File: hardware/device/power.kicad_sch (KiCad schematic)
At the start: 32 parts, among them J2 USB, U1 VOL_PWR_POT, U20 TPS62A02DRL, U21 TPS560200, U22 MAX17261xxTD, U23 BQ21040DBV, U26 FUSB303BTMX, U27 FUSB302B01MPX

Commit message: feat: add various connectors
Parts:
- added J1: POT_CONN, pocket_synth:CONN_503480-0540_MOL, symbol pocket_synth:5034800540
- added J4: FX6-20P-0.8SV1(71), pocket_synth:FX6-20P-0.8SV1(71), symbol pocket_synth:FX6-20P-0.8SV1(71)
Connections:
- net GND: now also J1.6 (MP), J1.7 (MP)
- net MCU_PWR_SW: now also J1.2; no longer U1.5 (SW)
- net VDD: now also J1.1; no longer U1.4 (SW)
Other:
- moved on the sheet: U1

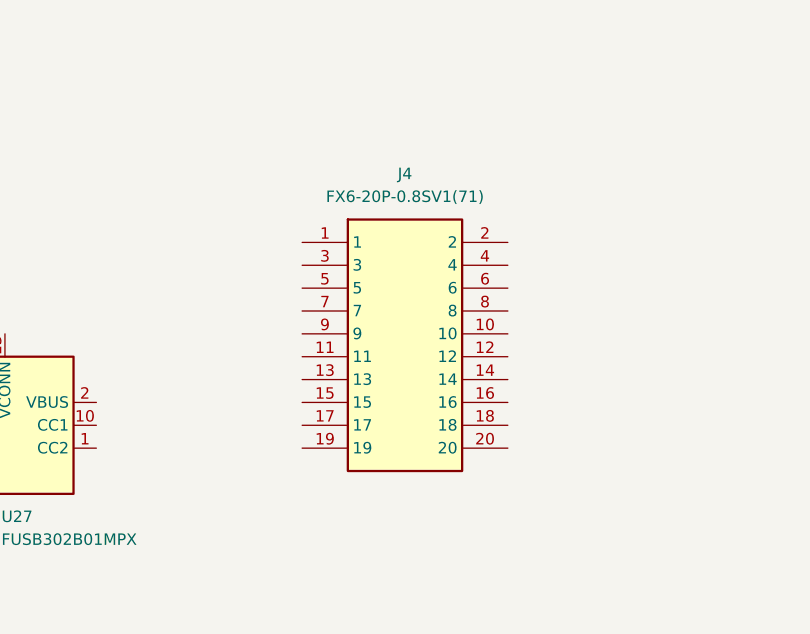
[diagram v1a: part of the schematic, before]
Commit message: feat: audio schematic, FMC bus, SDRAM connections
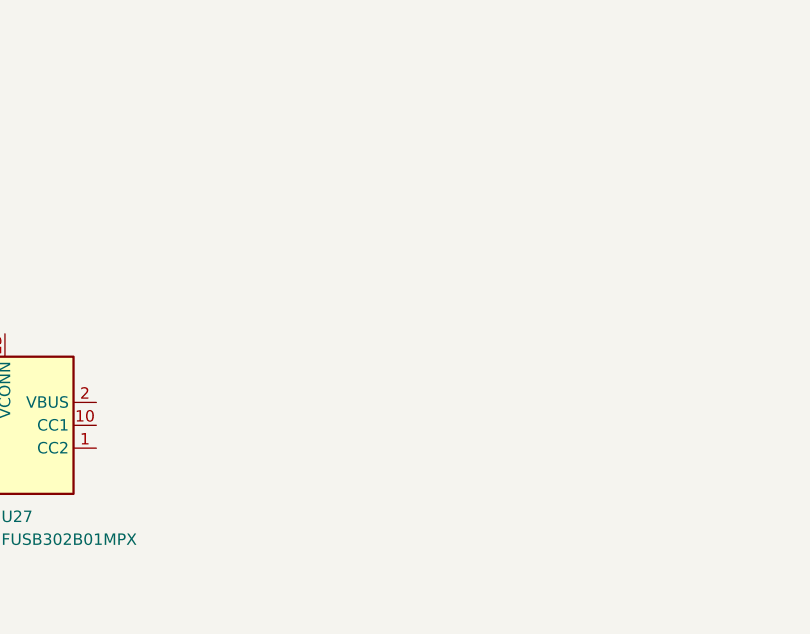
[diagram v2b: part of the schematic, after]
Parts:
- removed J4: FX6-20P-0.8SV1(71), pocket_synth:FX6-20P-0.8SV1(71), symbol pocket_synth:FX6-20P-0.8SV1(71)
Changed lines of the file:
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@@
-	)
-	(symbol
-		(lib_id "pocket_synth:FX6-20P-0.8SV1(71)")
-		(at 85.09 100.33 0)
-		(unit 1)
-		(exclude_from_sim no)
-		(in_bom yes)
-		(on_board yes)
-		(dnp no)
-		(fields_autoplaced yes)
-		(property "Reference" "J4"
-			(at 85.09 81.28 0)
-			(effects
-				(font
-					(size 1.27 1.27)
-				)
-			)
-		)
-		(property "Value" "FX6-20P-0.8SV1(71)"
-			(at 85.09 83.82 0)
-			(effects
-				(font
-					(size 1.27 1.27)
-				)
-			)
-		)
-		(property "Footprint" "pocket_synth:FX6-20P-0.8SV1(71)"
-			(at 92.71 183.82 0)
-			(effects
-				(font
-					(size 1.27 1.27)
-				)
-				(justify left top)
-				(hide yes)
-			)
-		)
-		(property "Datasheet" "https://www.hirose.com/en/product/p/CL0576-0021-0-71"
-			(at 92.71 283.82 0)
-			(effects
-				(font
-					(size 1.27 1.27)
-				)
-				(justify left top)
-				(hide yes)
-			)
-		)
-		(property "Description" "Hirose FX6 Series, 0.8mm Pitch 20 Way 2 Row Straight PCB Header, Solder Termination, 0.5A"
-			(at 85.09 100.33 0)
-			(effects
-				(font
-					(size 1.27 1.27)
-				)
-				(hide yes)
-			)
-		)
-		(property "Height" "6.25"
-			(at 92.71 483.82 0)
-			(effects
-				(font
-					(size 1.27 1.27)
-				)
-				(justify left top)
-				(hide yes)
-			)
-		)
-		(property "Mouser Part Number" "798-FX620P08SV171"
-			(at 92.71 583.82 0)
-			(effects
-				(font
-					(size 1.27 1.27)
-				)
-				(justify left top)
-				(hide yes)
-			)
-		)
-		(property "Mouser Price/Stock" "https://www.mouser.co.uk/ProductDetail/Hirose-Connector/FX6-20P-0.8SV171?qs=zOgoZG1CgI%2FdLW6QquT0oA%3D%3D"
-			(at 92.71 683.82 0)
-			(effects
-				(font
-					(size 1.27 1.27)
-				)
-				(justify left top)
-				(hide yes)
-			)
-		)
-		(property "Manufacturer_Name" "Hirose"
-			(at 92.71 783.82 0)
-			(effects
-				(font
-					(size 1.27 1.27)
-				)
-				(justify left top)
-				(hide yes)
-			)
-		)
-		(property "Manufacturer_Part_Number" "FX6-20P-0.8SV1(71)"
-			(at 92.71 883.82 0)
-			(effects
-				(font
-					(size 1.27 1.27)
-				)
-				(justify left top)
-				(hide yes)
-			)
-		)
-		(pin "16"
-		)
-		(pin "5"
-		)
-		(pin "12"
-		)
-		(pin "3"
-		)
-		(pin "15"
-		)
-		(pin "19"
-		)
-		(pin "10"
-		)
-		(pin "18"
-		)
-		(pin "14"
-		)
-		(pin "8"
-		)
-		(pin "1"
-		)
-		(pin "6"
-		)
-		(pin "4"
-		)
-		(pin "13"
-		)
-		(pin "2"
-		)
-		(pin "17"
-		)
-		(pin "11"
-		)
-		(pin "7"
-		)
-		(pin "9"
-		)
-		(pin "20"
-		)
-		(instances
-			(project ""
-				(path "/485383b8-00f4-4405-b270-de249939cff4/4ddef61a-efa7-4012-86d6-37c4f1088d14"
-					(reference "J4")
-					(unit 1)
-				)
-			)
-		)
 	)
 	(symbol

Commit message: feat: various layouts, changed SDRAM to BGA
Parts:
- removed C42: 10uf, Capacitor_SMD:C_0603_1608Metric_Pad1.08x0.95mm_HandSolder, symbol Device:C_Small
- removed U1: VOL_PWR_POT, pocket_synth:PTR901-2015K-B103, symbol pocket_synth:PTR901-2015K-B103
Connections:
- net GND: now also R2.2
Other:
- note added: "1v8 500mA Digital Supply"
- note added: "3v3 2A Digital Supply"
- note added: "Soft-Power Circuit & Volume Pot"
- note removed: "1v8 500mA Supply"
- note removed: "3v3 2A Supply"
- note removed: "TODO: MIDI over USB-C additional lines?"
- note removed: "TODO: ribbon cable connector"
- moved on the sheet: BT1, D17, D18, D19, J1, R1, R2, R3

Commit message: feat: various audio and power schematic layout
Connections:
- net USB_D+: now reaches J2.A6 (D+)
- net USB_D+: now also J2.B6 (D+)
- net USB_D-: now reaches J2.A7 (D-)
- net USB_D-: now also J2.B7 (D-)
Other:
- note added: "3.6-5.2v unregulated battery/charge voltage"
- note removed: "3.6-5.2v battery/charge voltage"
- moved on the sheet: D18, D19, J1, R1, R3

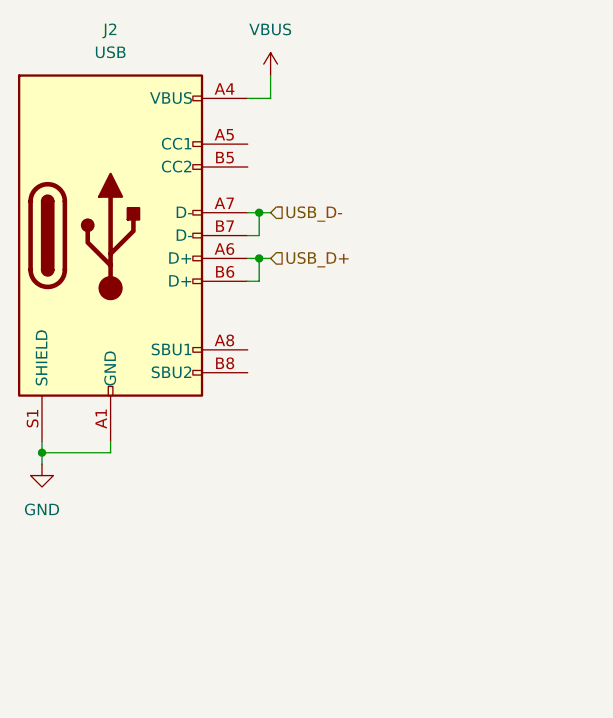
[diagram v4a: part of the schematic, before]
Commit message: feat: add audio routing muxes
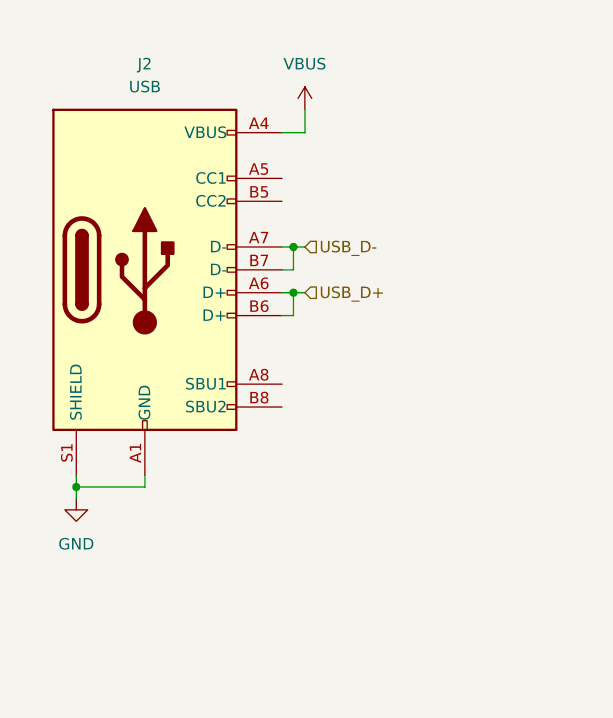
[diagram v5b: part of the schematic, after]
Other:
- moved on the sheet: J2
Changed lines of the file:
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@@
 	)
 	(junction
-		(at 17.78 62.23)
+		(at 21.59 66.04)
 		(diameter 0)
 		(color 0 0 0 0)
@@
 	)
 	(junction
-		(at 41.91 35.56)
+		(at 45.72 39.37)
 		(diameter 0)
 		(color 0 0 0 0)
 	)
 	(junction
-		(at 41.91 40.64)
+		(at 45.72 44.45)
 		(diameter 0)
 		(color 0 0 0 0)
@@
 	(wire
 		(pts
-			(xy 41.91 43.18) (xy 40.64 43.18)
+			(xy 45.72 46.99) (xy 44.45 46.99)
 		)
 		(stroke
@@
 	(wire
 		(pts
-			(xy 43.18 20.32) (xy 43.18 22.86)
+			(xy 46.99 24.13) (xy 46.99 26.67)
 		)
 		(stroke
@@
 	(wire
 		(pts
-			(xy 17.78 62.23) (xy 25.4 62.23)
+			(xy 21.59 66.04) (xy 29.21 66.04)
 		)
 		(stroke
@@
 	(wire
 		(pts
-			(xy 40.64 22.86) (xy 43.18 22.86)
+			(xy 44.45 26.67) (xy 46.99 26.67)
 		)
 		(stroke
@@
 	(wire
 		(pts
-			(xy 25.4 60.96) (xy 25.4 62.23)
+			(xy 29.21 64.77) (xy 29.21 66.04)
 		)
 		(stroke
@@
 	(wire
 		(pts
-			(xy 41.91 35.56) (xy 43.18 35.56)
+			(xy 45.72 39.37) (xy 46.99 39.37)
 		)
 		(stroke
@@
 	(wire
 		(pts
-			(xy 41.91 40.64) (xy 41.91 43.18)
+			(xy 45.72 44.45) (xy 45.72 46.99)
 		)
 		(stroke
@@
 	(wire
 		(pts
-			(xy 17.78 60.96) (xy 17.78 62.23)
+			(xy 21.59 64.77) (xy 21.59 66.04)
 		)
 		(stroke
@@
 	(wire
 		(pts
-			(xy 17.78 62.23) (xy 17.78 63.5)
+			(xy 21.59 66.04) (xy 21.59 67.31)
 		)
 		(stroke
@@
 	(wire
 		(pts
-			(xy 40.64 38.1) (xy 41.91 38.1)
+			(xy 44.45 41.91) (xy 45.72 41.91)
 		)
 		(stroke
@@
 	(wire
 		(pts
-			(xy 40.64 35.56) (xy 41.91 35.56)
+			(xy 44.45 39.37) (xy 45.72 39.37)
 		)
 		(stroke
@@
 	(wire
 		(pts
-			(xy 41.91 35.56) (xy 41.91 38.1)
+			(xy 45.72 39.37) (xy 45.72 41.91)
 		)
 		(stroke
@@
 	(wire
 		(pts
-			(xy 41.91 40.64) (xy 43.18 40.64)
+			(xy 45.72 44.45) (xy 46.99 44.45)
 		)
 		(stroke
@@
 	(wire
 		(pts
-			(xy 40.64 40.64) (xy 41.91 40.64)
+			(xy 44.45 44.45) (xy 45.72 44.45)
 		)
 		(stroke
@@
 	(hierarchical_label "USB_D+"
 		(shape input)
-		(at 43.18 40.64 0)
+		(at 46.99 44.45 0)
 		(effects
 			(font
@@
 	(hierarchical_label "USB_D-"
 		(shape input)
-		(at 43.18 35.56 0)
+		(at 46.99 39.37 0)
 		(effects
 			(font
@@
 	(symbol
 		(lib_id "power:GND")
-		(at 17.78 63.5 0)
+		(at 21.59 67.31 0)
 		(unit 1)
 		(exclude_from_sim no)
@@
 		(fields_autoplaced yes)
 		(property "Reference" "#PWR04"
-			(at 17.78 69.85 0)
+			(at 21.59 73.66 0)
 			(effects
 				(font
@@
 		)
 		(property "Value" "GND"
-			(at 17.78 68.58 0)
+			(at 21.59 72.39 0)
 			(effects
 				(font
@@
 		)
 		(property "Footprint" ""
-			(at 17.78 63.5 0)
+			(at 21.59 67.31 0)
 			(effects
 				(font
@@
 		)
 		(property "Datasheet" ""
-			(at 17.78 63.5 0)
+			(at 21.59 67.31 0)
 			(effects
 				(font
@@
 		)
 		(property "Description" "Power symbol creates a global label with name \"GND\" , ground"
-			(at 17.78 63.5 0)
+			(at 21.59 67.31 0)
 			(effects
 				(font
@@
 	(symbol
 		(lib_id "power:VBUS")
-		(at 43.18 20.32 0)
+		(at 46.99 24.13 0)
 		(unit 1)
 		(exclude_from_sim no)
@@
 		(fields_autoplaced yes)
 		(property "Reference" "#PWR05"
-			(at 43.18 24.13 0)
+			(at 46.99 27.94 0)
 			(effects
 				(font
@@
 		)
 		(property "Value" "VBUS"
-			(at 43.18 15.24 0)
+			(at 46.99 19.05 0)
 			(effects
 				(font
@@
 		)
 		(property "Footprint" ""
-			(at 43.18 20.32 0)
+			(at 46.99 24.13 0)
 			(effects
 				(font
@@
 		)
 		(property "Datasheet" ""
-			(at 43.18 20.32 0)
+			(at 46.99 24.13 0)
 			(effects
 				(font
@@
 		)
 		(property "Description" "Power symbol creates a global label with name \"VBUS\""
-			(at 43.18 20.32 0)
+			(at 46.99 24.13 0)
 			(effects
 				(font
@@
 	(symbol
 		(lib_id "Connector:USB_C_Receptacle_USB2.0_16P")
-		(at 25.4 38.1 0)
+		(at 29.21 41.91 0)
 		(unit 1)
 		(exclude_from_sim no)
@@
 		(fields_autoplaced yes)
 		(property "Reference" "J2"
-			(at 25.4 15.24 0)
+			(at 29.21 19.05 0)
 			(effects
 				(font
@@
 		)
 		(property "Value" "USB"
-			(at 25.4 17.78 0)
+			(at 29.21 21.59 0)
 			(effects
 				(font
@@
 		)
 		(property "Footprint" "Connector_USB:USB_C_Receptacle_G-Switch_GT-USB-7010ASV"
-			(at 29.21 38.1 0)
+			(at 33.02 41.91 0)
 			(effects
 				(font
@@
 		)
 		(property "Datasheet" "https://www.usb.org/sites/default/files/documents/usb_type-c.zip"
-			(at 29.21 38.1 0)
+			(at 33.02 41.91 0)
 			(effects
 				(font
@@
 		)
 		(property "Description" "USB 2.0-only 16P Type-C Receptacle connector"
-			(at 25.4 38.1 0)
+			(at 29.21 41.91 0)
 			(effects
 				(font
@@
 		)
 		(property "JLC" ""
-			(at 25.4 38.1 0)
+			(at 29.21 41.91 0)
 			(effects
 				(font

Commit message: feat: add ESD filter
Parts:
- added IC3: SP3401-02UTG, pocket_synth:SP340102UTG, symbol pocket_synth:SP3401-02UTG
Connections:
- net GND: now also IC3.3 (GND_1), IC3.4 (GND_2)
- net USB_D+: now also IC3.2 (I/O2), IC3.5 (NC_1)
- net USB_D-: now also IC3.1 (I/O1), IC3.6 (NC_2)
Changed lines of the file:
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@@
 	)
 	(junction
+		(at 73.66 66.04)
+		(diameter 0)
+		(color 0 0 0 0)
+	)
+	(junction
+		(at 45.72 41.91)
+		(diameter 0)
+		(color 0 0 0 0)
+	)
+	(junction
 		(at 166.37 31.75)
 		(diameter 0)
@@
 	)
 	(junction
-		(at 270.51 39.37)
+		(at 29.21 66.04)
 		(diameter 0)
 		(color 0 0 0 0)
 	)
 	(junction
-		(at 205.74 39.37)
+		(at 270.51 39.37)
 		(diameter 0)
 		(color 0 0 0 0)
 	)
 	(junction
-		(at 212.09 133.35)
+		(at 205.74 39.37)
 		(diameter 0)
 		(color 0 0 0 0)
 	)
 	(junction
-		(at 45.72 39.37)
+		(at 212.09 133.35)
 		(diameter 0)
 		(color 0 0 0 0)
@@
 	(wire
 		(pts
+			(xy 90.17 44.45) (xy 92.71 44.45)
+		)
+		(stroke
+			(width 0)
+			(type default)
+		)
+	)
+	(wire
+		(pts
+			(xy 73.66 66.04) (xy 29.21 66.04)
+		)
+		(stroke
+			(width 0)
+			(type default)
+		)
+	)
+	(wire
+		(pts
 			(xy 209.55 133.35) (xy 212.09 133.35)
 		)
@@
 	(wire
 		(pts
-			(xy 45.72 39.37) (xy 46.99 39.37)
+			(xy 45.72 41.91) (xy 59.69 41.91)
 		)
 		(stroke
@@
 	(wire
 		(pts
+			(xy 76.2 66.04) (xy 76.2 59.69)
+		)
+		(stroke
+			(width 0)
+			(type default)
+		)
+	)
+	(wire
+		(pts
 			(xy 128.27 43.18) (xy 128.27 48.26)
 		)
@@
 	(wire
 		(pts
+			(xy 90.17 41.91) (xy 92.71 41.91)
+		)
+		(stroke
+			(width 0)
+			(type default)
+		)
+	)
+	(wire
+		(pts
 			(xy 218.44 118.11) (xy 209.55 118.11)
 		)
@@
 	(wire
 		(pts
-			(xy 203.2 67.31) (xy 205.74 67.31)
+			(xy 45.72 39.37) (xy 45.72 41.91)
 		)
 		(stroke
@@
 	(wire
 		(pts
-			(xy 252.73 120.65) (xy 264.16 120.65)
+			(xy 203.2 67.31) (xy 205.74 67.31)
 		)
 		(stroke
@@
 	(wire
 		(pts
-			(xy 201.93 31.75) (xy 205.74 31.75)
+			(xy 252.73 120.65) (xy 264.16 120.65)
 		)
 		(stroke
@@
 	(wire
 		(pts
-			(xy 45.72 39.37) (xy 45.72 41.91)
+			(xy 201.93 31.75) (xy 205.74 31.75)
 		)
 		(stroke
@@
 	(wire
 		(pts
-			(xy 45.72 44.45) (xy 46.99 44.45)
+			(xy 45.72 44.45) (xy 59.69 44.45)
 		)
 		(stroke
@@
 	(wire
 		(pts
+			(xy 73.66 66.04) (xy 76.2 66.04)
+		)
+		(stroke
+			(width 0)
+			(type default)
+		)
+	)
+	(wire
+		(pts
 			(xy 205.74 31.75) (xy 205.74 33.02)
 		)
@@
 	(wire
 		(pts
+			(xy 73.66 59.69) (xy 73.66 66.04)
+		)
+		(stroke
+			(width 0)
+			(type default)
+		)
+	)
+	(wire
+		(pts
 			(xy 205.74 58.42) (xy 205.74 59.69)
 		)
@@
 		)
 	)
+	(label "USB_D+"
+		(at 46.99 44.45 0)
+		(effects
+			(font
+				(size 1.27 1.27)
+			)
+			(justify left bottom)
+		)
+	)
 	(label "3v3_PG"
 		(at 196.85 45.72 90)
@@
 		)
 	)
+	(label "USB_D-"
+		(at 46.99 41.91 0)
+		(effects
+			(font
+				(size 1.27 1.27)
+			)
+			(justify left bottom)
+		)
+	)
 	(label "PH_1v8"
 		(at 254 52.07 0)
@@
 	(hierarchical_label "USB_D+"
 		(shape input)
-		(at 46.99 44.45 0)
+		(at 92.71 44.45 0)
 		(effects
 			(font
@@
 	(hierarchical_label "USB_D-"
 		(shape input)
-		(at 46.99 39.37 0)
+		(at 92.71 41.91 0)
 		(effects
 			(font
@@
 					(unit 1)
 				)
+			)
+		)
+	)
+	(symbol
+		(lib_id "pocket_synth:SP3401-02UTG")
+		(at 74.93 46.99 0)
+		(unit 1)
+		(exclude_from_sim no)
+		(in_bom yes)
+		(on_board yes)
+		(dnp no)
+		(fields_autoplaced yes)
+		(property "Reference" "IC3"
+			(at 74.93 34.29 0)
+			(effects
+				(font
+					(size 1.27 1.27)
+				)
+			)
+		)
+		(property "Value" "SP3401-02UTG"
+			(at 74.93 36.83 0)
+			(effects
+				(font
+					(size 1.27 1.27)
+				)
+			)
+		)
+		(property "Footprint" "pocket_synth:SP340102UTG"
+			(at 101.6 141.91 0)
+			(effects
+				(font
+					(size 1.27 1.27)
+				)
+				(justify left top)
+				(hide yes)
+			)
+		)
+		(property "Datasheet" "https://m.littelfuse.com/~/media/electronics/datasheets/tvs_diode_arrays/littelfuse_tvs_diode_array_sp3401_datasheet.pdf.pdf"
+			(at 101.6 241.91 0)
+			(effects
+				(font
+					(size 1.27 1.27)
+				)
+				(justify left top)
+				(hide yes)
+			)
+		)
+		(property "Description" "ESD Suppressors / TVS Diodes 28KV 0.6pF 3.3V 10A uDFN-6 TVS Array"
+			(at 74.93 46.99 0)
+			(effects
+				(font
+					(size 1.27 1.27)
+				)
+				(hide yes)
+			)
+		)
+		(property "Height" "0.55"
+			(at 101.6 441.91 0)
+			(effects
+				(font
+					(size 1.27 1.27)
+				)
+				(justify left top)
+				(hide yes)
+			)
+		)
+		(property "Mouser Part Number" "576-SP3401-02UTG"
+			(at 101.6 541.91 0)
+			(effects
+				(font
+					(size 1.27 1.27)
+				)
+				(justify left top)
+				(hide yes)
+			)
+		)
+		(property "Mouser Price/Stock" "https://www.mouser.co.uk/ProductDetail/Littelfuse/SP3401-02UTG?qs=T3oQrply3y%2FjRDLmSQJ5ww%3D%3D"
+			(at 101.6 641.91 0)
+			(effects
+				(font
+					(size 1.27 1.27)
+				)
+				(justify left top)
+				(hide yes)
+			)
+		)
+		(property "Manufacturer_Name" "LITTELFUSE"
+			(at 101.6 741.91 0)
+			(effects
+				(font
+					(size 1.27 1.27)
+				)
+				(justify left top)
+				(hide yes)
+			)
+		)
+		(property "Manufacturer_Part_Number" "SP3401-02UTG"
+			(at 101.6 841.91 0)
+			(effects
+				(font
+					(size 1.27 1.27)
+				)
+				(justify left top)
+				(hide yes)
+			)
+		)
+		(pin "5"
+		)
+		(pin "2"
+		)
+		(pin "3"
+		)
+		(pin "4"
+		)
+		(pin "1"
+		)
+		(pin "6"
+		)
+		(instances
+			(project ""
+				(path "/485383b8-00f4-4405-b270-de249939cff4/4ddef61a-efa7-4012-86d6-37c4f1088d14"
+					(reference "IC3")
+					(unit 1)
+				)

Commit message: feat: power schematic cleanup, add USB PD controller
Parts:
- removed C39, C41: 10uf, Capacitor_SMD:C_0603_1608Metric_Pad1.08x0.95mm_HandSolder, symbol Device:C_Small
- removed C40: 0.1uf, Capacitor_SMD:C_0603_1608Metric_Pad1.08x0.95mm_HandSolder, symbol Device:C_Small
- removed C48: 120pF, Capacitor_SMD:C_0603_1608Metric_Pad1.08x0.95mm_HandSolder, symbol Device:C_Small
- removed C49: 22uf, Capacitor_SMD:C_0603_1608Metric_Pad1.08x0.95mm_HandSolder, symbol Device:C_Small
- removed C50: 4.7uf, Capacitor_SMD:C_0603_1608Metric_Pad1.08x0.95mm_HandSolder, symbol Device:C_Small
- removed L3: 10uh, Inductor_SMD:L_0603_1608Metric_Pad1.05x0.95mm_HandSolder, symbol Device:L_Small
- removed L7: 1uh, Inductor_SMD:L_0603_1608Metric_Pad1.05x0.95mm_HandSolder, symbol Device:L_Small
- removed R29: 442k, Resistor_SMD:R_0603_1608Metric_Pad0.98x0.95mm_HandSolder, symbol Device:R_Small
- removed R54: 97.6k, Resistor_SMD:R_0603_1608Metric_Pad0.98x0.95mm_HandSolder, symbol Device:R_Small
- removed R55: 24.9k, Resistor_SMD:R_0603_1608Metric_Pad0.98x0.95mm_HandSolder, symbol Device:R_Small
- removed R56: 20.0k, Resistor_SMD:R_0603_1608Metric_Pad0.98x0.95mm_HandSolder, symbol Device:R_Small
- added C11: 22uF, symbol Device:C_Small
- added C12: 22uF, symbol Device:C
- added C13: 120pF, symbol Device:C
- added C14, C16: 10uF, symbol Device:C
- added C15: 0.1uF, symbol Device:C
- added C9: 4.7uF, symbol Device:C
- added D21: 1v8_PWR, LED_SMD:LED_0805_2012Metric_Pad1.15x1.40mm_HandSolder, symbol Device:LED
- added L1: 1uH, symbol Device:L
- added L2: 10uH, symbol Device:L
- added R12: 100R, symbol Device:R_Small
- added R20: 165R, symbol Device:R
- added R21: 97.6k, symbol Device:R
- added R23: 442, symbol Device:R
- added R24: 20k, symbol Device:R
- added R26: 24.9k, symbol Device:R
- added R27: 25R, symbol Device:R
- added U31: FUSB302B01MPX, Package_DFN_QFN:WQFN-14-1EP_2.5x2.5mm_P0.5mm_EP1.45x1.45mm, symbol Interface_USB:FUSB302B01MPX
- D17: value PWR -> 3v3_PWR; Color (none) -> RED
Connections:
- net +1V8: now also C16.1, D21.2 (A), L2.2, R26.1
- net +3.3V: now also C12.1, C13.1, C14.1, C15.1, L1.2, R12.1, R23.1, U31.3 (VDD), U31.4 (VDD)
- net GND: now also C12.2, C14.2, C15.2, C16.2, C9.2, R21.2, R24.2, R27.2, U31.15 (GND), U31.8 (GND), U31.9 (GND)
- net MCU_PWR_SW: now also R20.2; no longer D18.2 (A), J1.2, R1.1
- net VBUS: now also U31.2 (VBUS)
- net VDD: now also C9.1
- net at U20.2 (SW): now also L1.1
- net at U20.5 (FB): now also C13.2, R21.1, R23.2
- net at U21.3 (PH): now also L2.1
- net at U21.5 (FB): now also R24.1, R26.2
- net VOL_A: now reaches J1.3
- net VOL_A: now also C11.1, R12.2
- net VOL_POT: now reaches J1.4
- net VOL_C: now reaches J1.5
- net VOL_C: now also C11.2
- net at J2.A5 (CC1): now also U31.10 (CC1), U31.14 (CC2)
- net at J2.B5 (CC2): now also U31.1 (CC2)
- new net: D18.2 (A), J1.2, R1.1, R20.1
- new net: D21.1 (K), R27.1
- new net I2C.SCL: U31.6 (SCL)
- new net I2C.SDA: U31.7 (SDA)
- new net USB_INT: U31.5 (INT_N)
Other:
- note added: "165R causes 1.9v drop at 20ma to make VDD voltage 3.3 MCU tolerant to read state."
- note added: "Charger supply and USB High-Speed"
- note added: "Diodes prevent backflow of the VDD always-on voltage back to the 3.3v tollerant MCU pins."
- note added: "ESD filter on USB differential pair."
- note added: "Potentiometer RC Filter"
- note added: "Primarily for memory"
- note added: "Pull-downs ensure enable signal isn't floating."
- note added: "RC filter with an FC of 72Hz to alleviate SMPS noise on the potentiometer."
- note added: "Regulator EN is toggled by the soft power-off circuit tied to the volume+power knob and MCU."
- note added: "Soft-Power Enable & Volume Pot"
- note added: "USB PD and mode IC"
- note added: "USB-C Connector"
- note removed: "3.3v GPIO-based soft power off enable"
- note removed: "NOTE: Chained with the primary 3.3v SMPS"
- note removed: "Reads power switch state"
- note removed: "Soft-Power Circuit & Volume Pot"
- moved on the sheet: BT1, D17, D18, D19, J1, J2, R1, R2, R3, R63, R72, TP14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
